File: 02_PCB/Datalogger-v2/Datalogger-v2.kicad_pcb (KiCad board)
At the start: 2 copper layers, 92.4 x 86.4 mm, 27 parts, among them SW1 SW_Push, U1 Micro SD Card Adapter, U8 ESP32 DEV KIT DOIT

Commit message: Update PCB layout
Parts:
- removed U3: ~, Datalogger-v2:WT901B
- added REF**: WT901B, Datalogger-v2:WT901B, F.Cu at (139.0, 65.0)
- moved ? 1.42 mm to (72.5, 70.4)
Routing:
- net +5V: track 0.00 -> 149.3 mm
- net +3.3V: track 0.00 -> 79.0 mm
- net Net-(U3-SDA): track 0.00 -> 44.9 mm

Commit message: Update footprints and library
- Added missing footprint library files
- Changed footprints
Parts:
- moved U5 5.94 mm to (89.8, 65.3)
- moved U8 5.85 mm to (104.7, 95.8)
- renumbered REF** to U3

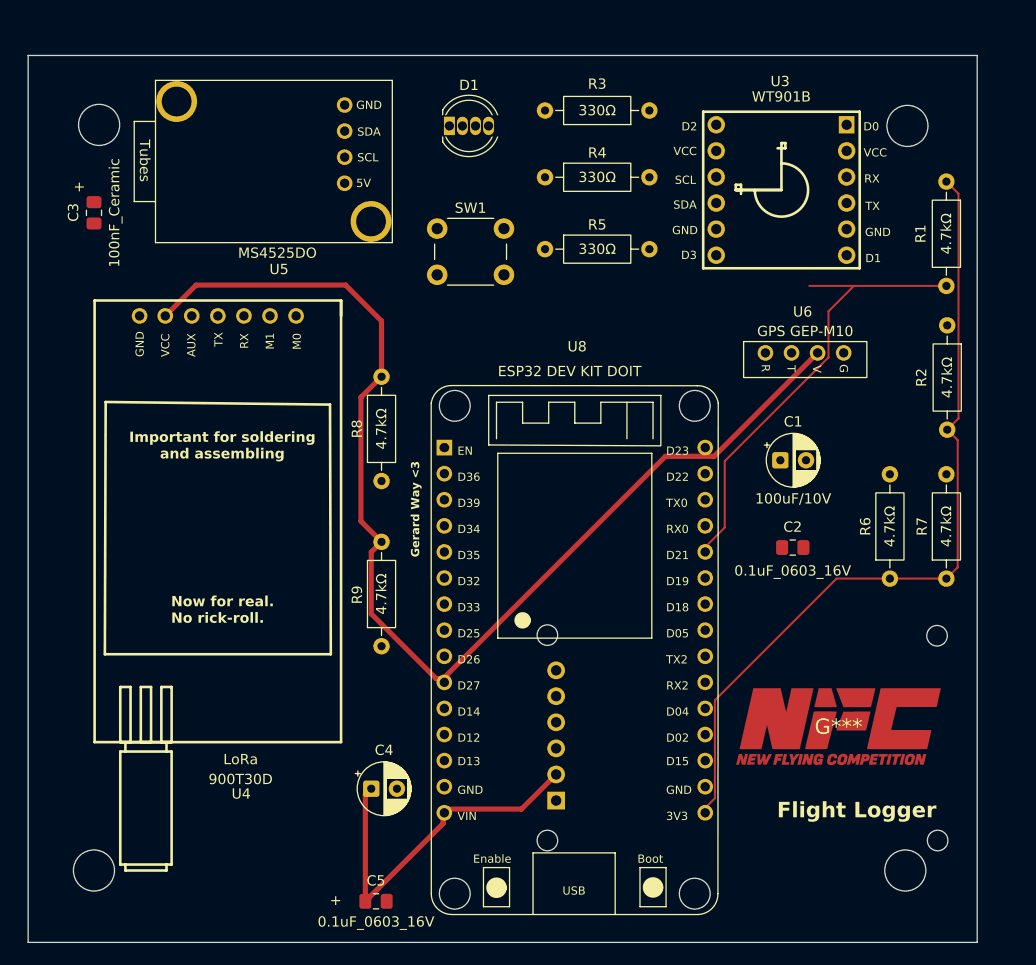
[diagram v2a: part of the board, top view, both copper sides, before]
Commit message: Update PCB layout and footprints library
- Sync schematic and PCB
- Fixed more errors in footprints library
- Updated PCB layout
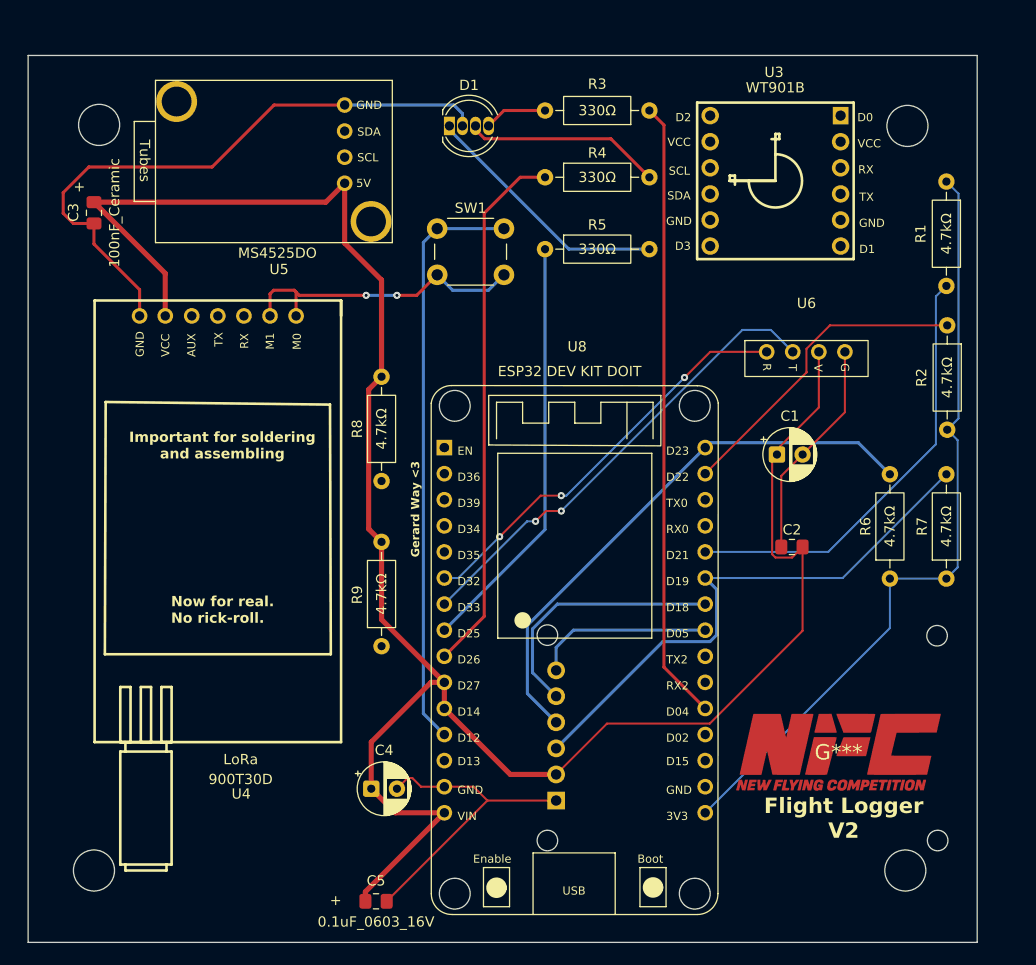
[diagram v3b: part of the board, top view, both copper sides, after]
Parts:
- U3: value WT901B -> ~
- moved G*** 2.50 mm to (144.5, 131.5)
- moved U3 1.07 mm to (138.4, 64.1)
- moved C1 0.65 mm to (138.5, 102.5)
- moved U6 0.16 mm to (141.4, 93.4)
- moved C2 0.09 mm to (140.0, 111.5), turned to 0 degrees
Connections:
- U3 pad 1: (no net) -> unconnected-(U3-D0-Pad1)
- U3 pad 10: (no net) -> Net-(U3-SDA)
- U3 pad 11: (no net) -> GND
- U3 pad 12: (no net) -> unconnected-(U3-D3-Pad12)
- U3 pad 2: (no net) -> unconnected-(U3-VCC-Pad2)
- U3 pad 3: (no net) -> unconnected-(U3-RX-Pad3)
- U3 pad 4: (no net) -> unconnected-(U3-TX-Pad4)
- U3 pad 5: (no net) -> unconnected-(U3-GND-Pad5)
- U3 pad 6: (no net) -> unconnected-(U3-D1-Pad6)
- U3 pad 7: (no net) -> unconnected-(U3-D2-Pad7)
- U3 pad 8: (no net) -> +5V
- U3 pad 9: (no net) -> Net-(U3-SCL)
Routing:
- net GND: track 0.00 -> 142.2 mm, vias 0 -> 2
- net Net-(U8-ADC/D4): track 0.00 -> 60.5 mm
- net Net-(U8-ADC/D12): track 0.00 -> 57.2 mm
- net +5V: track 149.3 -> 205.9 mm
- net Net-(U1-MOSI): track 0.00 -> 54.5 mm
- net Net-(U1-MISO): track 0.00 -> 53.9 mm
- net Net-(U8-ADC/DAC1/D26): track 0.00 -> 52.1 mm
- net Net-(U6-TX): track 0.00 -> 45.9 mm, vias 0 -> 2
- net Net-(U8-ADC/DAC0/D25): track 0.00 -> 41.2 mm
- net Net-(U6-RX): track 0.00 -> 40.5 mm, vias 0 -> 3
- net Net-(U3-SCL): track 0.00 -> 30.9 mm
- net Net-(U1-SCK): track 0.00 -> 25.3 mm
- net Net-(D1-DO): track 0.00 -> 24.7 mm
- net Net-(D1-VDD): track 0.00 -> 19.2 mm
- net Net-(U1-CS): track 0.00 -> 17.4 mm
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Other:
- board text added: "Flight Logger V2"
- board text added: "Tracks width: - 5 V power: 0.8 mm - 3.3 V power: 0.2 mm - ESP32/LoRa power: 0.5 mm - SPI/UART/I2C/GPIO: 0.2 mm - Resistors/capacitors: 0.3 mm - SD Card: 0.3 mm - Ground: 0.2 mm Vias: 0.7 mm / 0.3 mm drill"
- board text removed: "Flight Logger"
- board text removed: "Tracks width: - 5 V power: 0.8 mm - 3.3 V power: 0.2 mm - ESP32/LoRa power: 0.5 mm - SPI/UART/I2C/GPIO: 0.2 mm - Resistors/capacitors: 0.2 mm - SD Card: 0.3 mm Vias: 0.7 mm / 0.3 mm drill"

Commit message: Update PCB layout
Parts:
- moved U3 0.59 mm to (139.0, 64.1)
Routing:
- net Net-(U4-TX): track 0.00 -> 85.5 mm, vias 0 -> 2
- net Net-(U4-RX): track 0.00 -> 68.9 mm, vias 0 -> 4
- net Net-(U5-SCL): track 0.00 -> 51.8 mm
- net Net-(U5-SDA): track 0.00 -> 38.0 mm
- net Net-(U3-SDA): track 42.6 -> 75.2 mm
- net GND: track 142.2 -> 170.7 mm, vias 2 -> 3
- net +5V: track 205.9 -> 230.5 mm
- net Net-(U3-SCL): track 30.9 -> 50.8 mm
- net Net-(U1-MISO): track 53.9 -> 55.4 mm
